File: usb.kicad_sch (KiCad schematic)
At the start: 11 parts, among them J3 CX90B1-24P, U3 CY7C65215-32LTXI, U8 TPD4E004DRYR

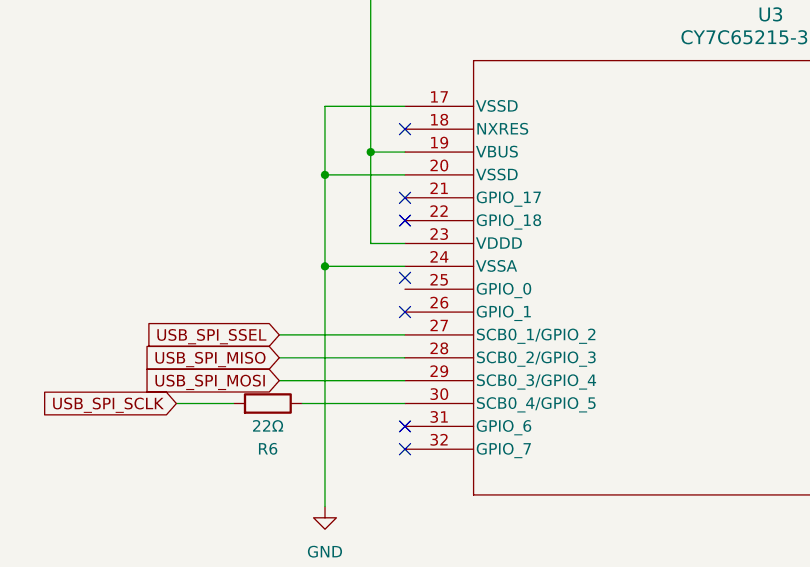
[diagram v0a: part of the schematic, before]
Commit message: Clean up schematics
Signed-off-by: Corey Minyard <corey@minyard.net>
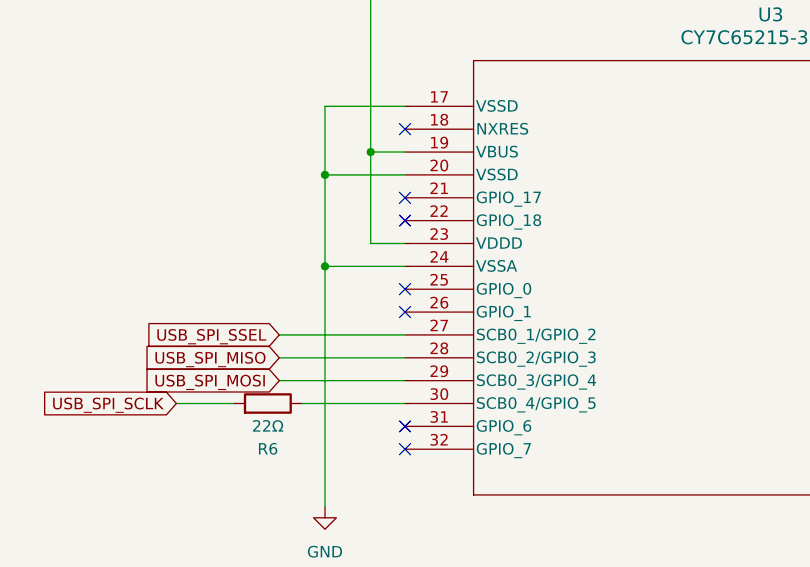
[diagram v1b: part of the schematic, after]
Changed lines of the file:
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@@
 	)
 	(no_connect
-		(at 55.88 116.84)
+		(at 55.88 118.11)
 	)
 	(no_connect
@@
 		(pin "11"
 		)
-	)
+		(instances
+			(project ""
+				(path "/23e49ab9-97e0-460a-806c-ff6f37958474/a401ed87-a6b2-451c-b983-d48d83161fe4"
+					(reference "U3")
+					(unit 1)
+				)
+			)
+		)
+	)

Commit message: Start on PCB
Clean up a lot of issues.

Signed-off-by: Corey Minyard <corey@minyard.net>
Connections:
- net GND: now also U3.33 (GND/PAD)
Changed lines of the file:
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@@
+	)
+	(junction
+		(at 46.99 97.79)
+		(diameter 0)
+		(color 0 0 0 0)
 	)
 	(junction
@@
 		(pts
 			(xy 137.16 107.95) (xy 151.13 107.95)
+		)
+		(stroke
+			(width 0)
+			(type default)
+		)
+	)
+	(wire
+		(pts
+			(xy 55.88 95.25) (xy 46.99 95.25)
+		)
+		(stroke
+			(width 0)
+			(type default)
+		)
+	)
+	(wire
+		(pts
+			(xy 46.99 95.25) (xy 46.99 97.79)
 		)
 		(stroke
@@
 		(pin "11"
 		)
+		(pin "33"
+		)
 		(instances

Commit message: Finish layout
Signed-off-by: Corey Minyard <corey@minyard.net>
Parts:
- added C82, C83, C84: 100nF, Capacitor_SMD:C_0402_1005Metric, symbol Device:C
- added R21, R22: 0Ω, Resistor_SMD:R_0402_1005Metric, symbol Device:R
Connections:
- net +3.3V: now also C82.2, C83.2, C84.2
- net GND: now also C82.1, C83.1, C84.1
- net USB_RX: now also R22.2; no longer U3.5 (SCB1_0/GPIO_10)
- net USB_TX: now also R21.2; no longer U3.6 (SCB1_1/GPIO_11)
- new net: R22.1, U3.5 (SCB1_0/GPIO_10)
- new net: R21.1, U3.6 (SCB1_1/GPIO_11)

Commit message: Add pull up on the PA enables
So they are off by default.

Signed-off-by: Corey Minyard <corey@minyard.net>
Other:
- note added: "Main USB connector. If the connection is capable of supplying 3A at 5V, you can use this for power by installing J9."
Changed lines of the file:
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@@
+		)
+	)
+	(text "Main USB connector.  If the\nconnection is capable of\nsupplying 3A at 5V, you can\nuse this for power by installing\nJ9."
+		(exclude_from_sim no)
+		(at 213.614 33.528 0)
+		(effects
+			(font
+				(size 1.27 1.27)
+			)
 		)
 	)

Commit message: Make a bunch of GPIOs more easily available
Put them on DNP zero-ohm resistors.

Signed-off-by: Corey Minyard <corey@minyard.net>
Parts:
- added R41, R42: 0Ω, Resistor_SMD:R_0402_1005Metric, symbol Device:R
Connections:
- net at U3.25 (GPIO_0): now also R41.1
- net at U3.26 (GPIO_1): now also R42.1
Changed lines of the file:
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@@
 	)
 	(no_connect
-		(at 55.88 120.65)
-	)
-	(no_connect
 		(at 194.31 62.23)
 	)
@@
 	)
 	(no_connect
+		(at 35.56 118.11)
+	)
+	(no_connect
 		(at 137.16 115.57)
 	)
@@
 	)
 	(no_connect
-		(at 55.88 118.11)
+		(at 35.56 120.65)
 	)
 	(no_connect
@@
 	(wire
 		(pts
+			(xy 43.18 120.65) (xy 55.88 120.65)
+		)
+		(stroke
+			(width 0)
+			(type default)
+		)
+	)
+	(wire
+		(pts
 			(xy 46.99 115.57) (xy 55.88 115.57)
 		)
@@
 	(wire
 		(pts
+			(xy 43.18 118.11) (xy 55.88 118.11)
+		)
+		(stroke
+			(width 0)
+			(type default)
+		)
+	)
+	(wire
+		(pts
 			(xy 148.59 88.9) (xy 148.59 91.44)
 		)
@@
 	)
 	(symbol
+		(lib_id "Device:R")
+		(at 39.37 118.11 270)
+		(unit 1)
+		(exclude_from_sim no)
+		(in_bom no)
+		(on_board yes)
+		(dnp yes)
+		(property "Reference" "R41"
+			(at 34.544 116.586 90)
+			(effects
+				(font
+					(size 1.27 1.27)
+				)
+			)
+		)
+		(property "Value" "0Ω"
+			(at 43.688 116.586 90)
+			(effects
+				(font
+					(size 1.27 1.27)
+				)
+			)
+		)
+		(property "Footprint" "Resistor_SMD:R_0402_1005Metric"
+			(at 39.37 116.332 90)
+			(effects
+				(font
+					(size 1.27 1.27)
+				)
+				(hide yes)
+			)
+		)
+		(property "Datasheet" "~"
+			(at 39.37 118.11 0)
+			(effects
+				(font
+					(size 1.27 1.27)
+				)
+				(hide yes)
+			)
+		)
+		(property "Description" "Resistor"
+			(at 39.37 118.11 0)
+			(effects
+				(font
+					(size 1.27 1.27)
+				)
+				(hide yes)
+			)
+		)
+		(pin "2"
+		)
+		(pin "1"
+		)
+		(instances
+			(project "FSKGroundStation"
+				(path "/23e49ab9-97e0-460a-806c-ff6f37958474/a401ed87-a6b2-451c-b983-d48d83161fe4"
+					(reference "R41")
+					(unit 1)
+				)
+			)
+		)
+	)
+	(symbol
 		(lib_id "power:GND")
 		(at 177.8 83.82 0)
@@
 					(unit 1)
 				)
+			)
+		)
+	)
+	(symbol
+		(lib_id "Device:R")
+		(at 39.37 120.65 270)
+		(unit 1)
+		(exclude_from_sim no)
+		(in_bom no)
+		(on_board yes)
+		(dnp yes)
+		(property "Reference" "R42"
+			(at 34.544 119.126 90)
+			(effects
+				(font
+					(size 1.27 1.27)
+				)
+			)
+		)
+		(property "Value" "0Ω"
+			(at 43.688 119.126 90)
+			(effects
+				(font
+					(size 1.27 1.27)
+				)
+			)
+		)
+		(property "Footprint" "Resistor_SMD:R_0402_1005Metric"
+			(at 39.37 118.872 90)
+			(effects
+				(font
+					(size 1.27 1.27)
+				)
+				(hide yes)
+			)
+		)
+		(property "Datasheet" "~"
+			(at 39.37 120.65 0)
+			(effects
+				(font
+					(size 1.27 1.27)
+				)
+				(hide yes)
+			)
+		)
+		(property "Description" "Resistor"
+			(at 39.37 120.65 0)
+			(effects
+				(font
+					(size 1.27 1.27)
+				)
+				(hide yes)
+			)
+		)
+		(pin "2"
+		)
+		(pin "1"
+		)
+		(instances
+			(project "FSKGroundStation"
+				(path "/23e49ab9-97e0-460a-806c-ff6f37958474/a401ed87-a6b2-451c-b983-d48d83161fe4"
+					(reference "R42")
+					(unit 1)
+				)

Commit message: Finish initial layet
Signed-off-by: Corey Minyard <corey@minyard.net>
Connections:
- net USB_SPI_DATA_READY: no longer names the net of U3.2 (SCB0_0/GPIO_8)
- no-connect marks 23 -> 24
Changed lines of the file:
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@@
+	)
+	(no_connect
+		(at 137.16 133.35)
 	)
 	(no_connect
@@
 		(pts
 			(xy 246.38 44.45) (xy 217.17 44.45)
-		)
-		(stroke
-			(width 0)
-			(type default)
-		)
-	)
-	(wire
-		(pts
-			(xy 137.16 133.35) (xy 151.13 133.35)
 		)
 		(stroke
@@
 				(hide yes)
 			)
-		)
-	)
-	(global_label "USB_SPI_DATA_READY"
-		(shape input)
-		(at 151.13 133.35 0)
-		(fields_autoplaced yes)
-		(effects
-			(font
-				(size 1.27 1.27)
-			)
-			(justify left)
-		)
-		(property "Intersheetrefs" "${INTERSHEET_REFS}"
-			(at 174.1933 133.35 0)
-			(effects
-				(font
-					(size 1.27 1.27)
-				)
-				(justify left)
-				(hide yes)
-			)

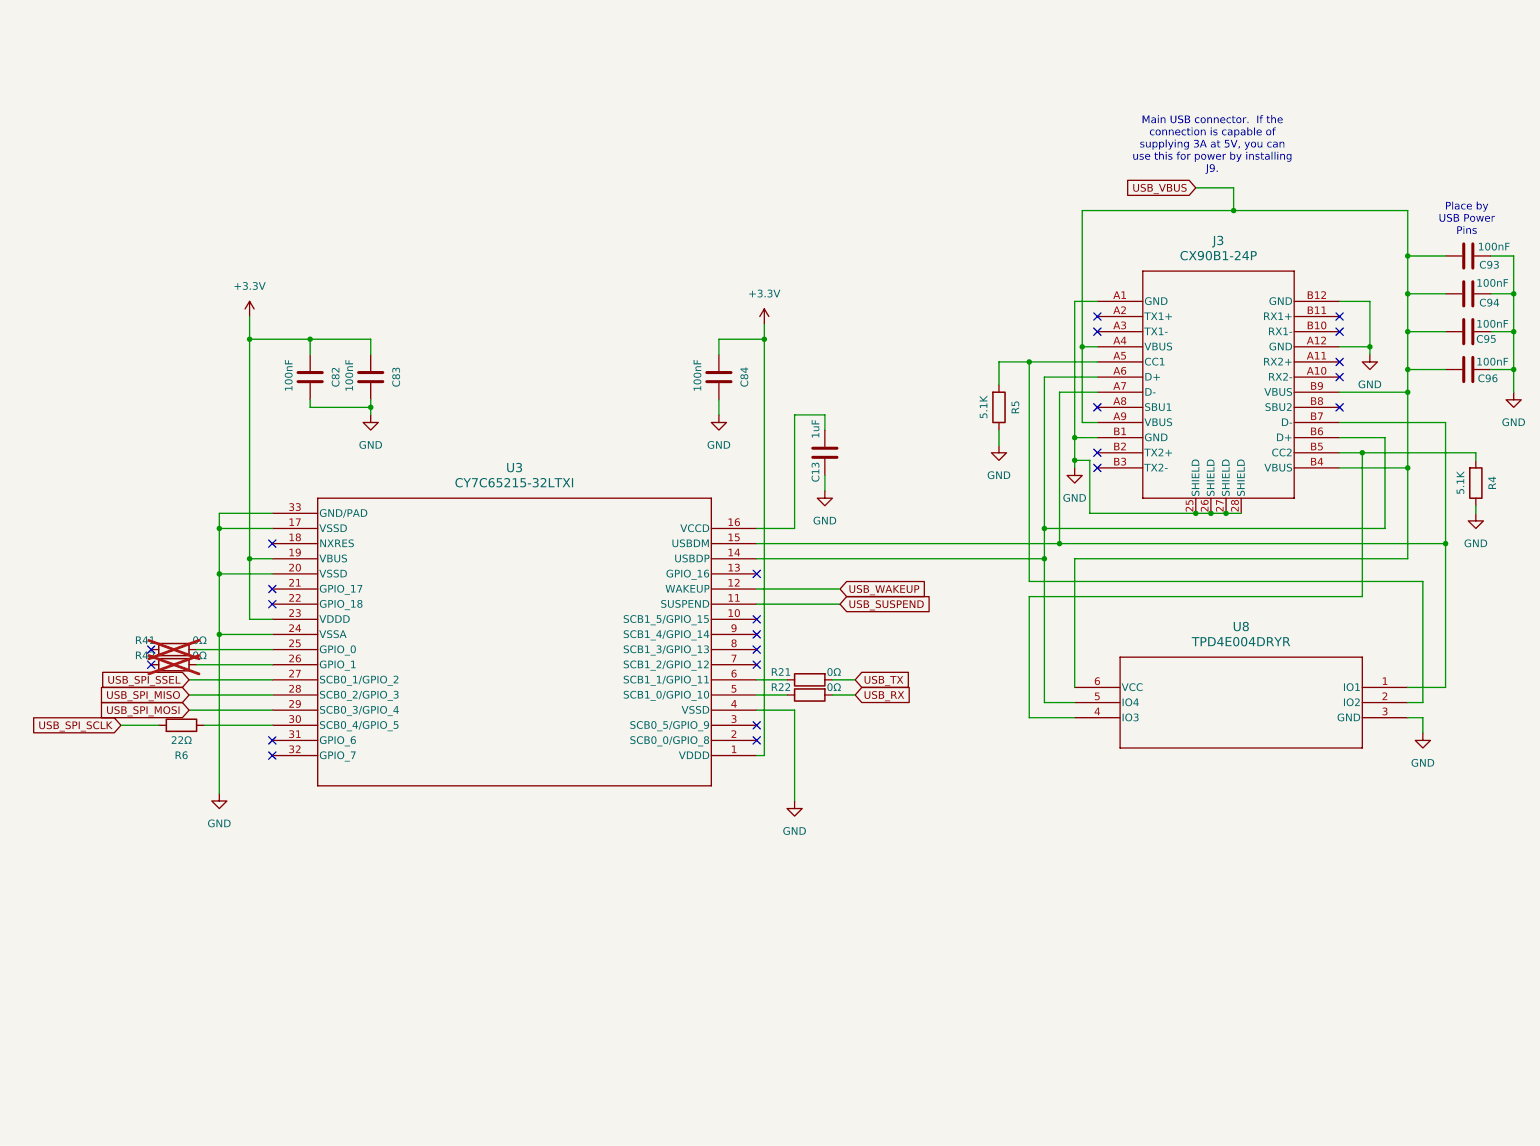
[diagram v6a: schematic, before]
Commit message: Switch to a CPU with a USB interface for the USB connection
The part that was picked had proprietary tools and configuration and it
didn't support interrupts.  The CPU is cheaper and more capable.

Signed-off-by: Corey Minyard <corey@minyard.net>
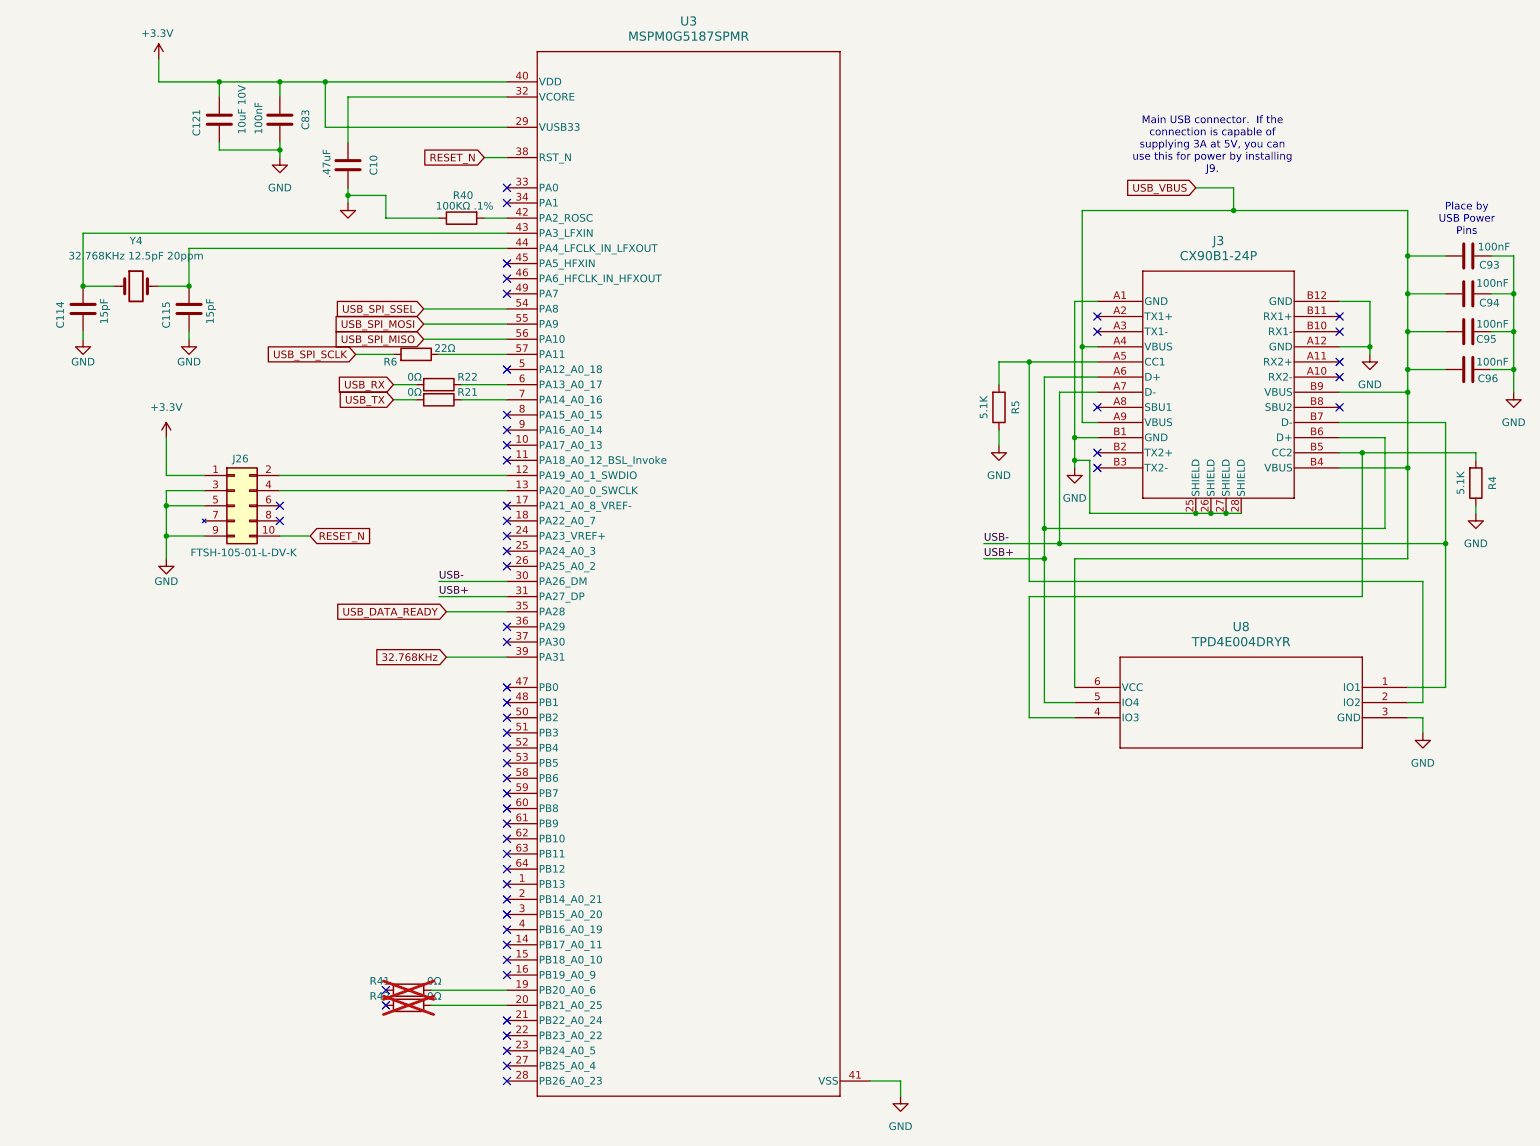
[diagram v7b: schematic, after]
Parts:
- removed C13: 1uF, Capacitor_SMD:C_0603_1608Metric_Pad1.08x0.95mm_HandSolder, symbol Device:C
- removed C82, C84: 100nF, Capacitor_SMD:C_0402_1005Metric, symbol Device:C
- removed U3: CY7C65215-32LTXI, footprints:PG-VQFN-32-803, symbol Local ICs:CY7C65215-32LTXI
- added C10: .47uF, Capacitor_SMD:C_0603_1608Metric_Pad1.08x0.95mm_HandSolder, symbol Device:C
- added C114, C115: 15pF, Capacitor_SMD:C_0402_1005Metric_Pad0.74x0.62mm_HandSolder, symbol Device:C
- added C121: 10uF 10V, Capacitor_SMD:C_1206_3216Metric_Pad1.33x1.80mm_HandSolder, symbol Device:C
- added J26: FTSH-105-01-L-DV-K, footprints:FTSH-105-01-L-DV-K, symbol Local Connectors:ARM CM10 JTAG
- added R40: 100KΩ .1%, Resistor_SMD:R_0402_1005Metric, symbol Device:R
- added U3: MSPM0G5187SPMR, footprints:PM0064A-IPC_A, symbol Local ICs:MSPM0G5187SPMR
- added Y4: 32.768KHz 12.5pF 20ppm, Crystal:Crystal_SMD_2012-2Pin_2.0x1.2mm, symbol Device:Crystal
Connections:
- net +3.3V: now also C121.2, J26.1 (VTREF), U3.29 (VUSB33), U3.40 (VDD)
- net GND: now also C10.1, C114.1, C115.1, C121.1, J26.3 (GND), J26.5 (GND), J26.9 (GND), R40.1, U3.41 (VSS)
- net USB_SPI_MISO: now also U3.56 (PA10)
- net USB_SPI_MOSI: now also U3.55 (PA9)
- net USB_SPI_SSEL: now also U3.54 (PA8)
- net USB+: now reaches J3.A6 (D+), J3.B6 (D+), U8.5 (IO4)
- net USB+: now also U3.31 (PA27_DP)
- net USB-: now reaches J3.A7 (D-), J3.B7 (D-), U8.1 (IO1)
- net USB-: now also U3.30 (PA26_DM)
- net at R41.1: now also U3.19 (PB20_A0_6)
- net at R42.1: now also U3.20 (PB21_A0_25)
- net at R6.1: now also U3.57 (PA11)
- net at R22.1: now also U3.6 (PA13_A0_17)
- net at R21.1: now also U3.7 (PA14_A0_16)
- new net: J26.2 (TMS), U3.12 (PA19_A0_1_SWDIO)
- new net: J26.4 (TCK), U3.13 (PA20_A0_0_SWCLK)
- new net: C115.2, U3.44 (PA4_LFCLK_IN_LFXOUT), Y4.2
- new net: C10.2, U3.32 (VCORE)
- new net: C114.2, U3.43 (PA3_LFXIN), Y4.1
- new net: R40.2, U3.42 (PA2_ROSC)
- new net 32.768KHz: U3.39 (PA31)
- new net RESET_N: J26.10 (NRST), U3.38 (RST_N)
- new net USB_DATA_READY: U3.35 (PA28)
- no-connect marks 24 -> 56
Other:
- moved on the sheet: C83, R21, R22, R41, R42, R6

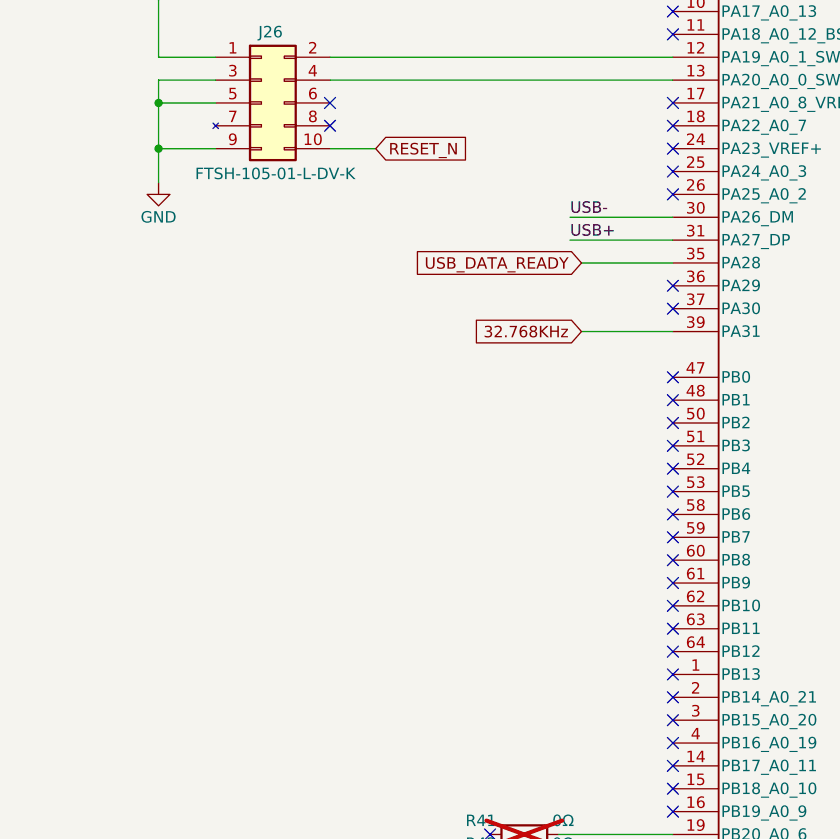
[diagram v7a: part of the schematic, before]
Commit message: Add a clock from the USB chip to the FPGA
The FPGA might need a clock for certain things, so provide it.

Signed-off-by: Corey Minyard <corey@minyard.net>
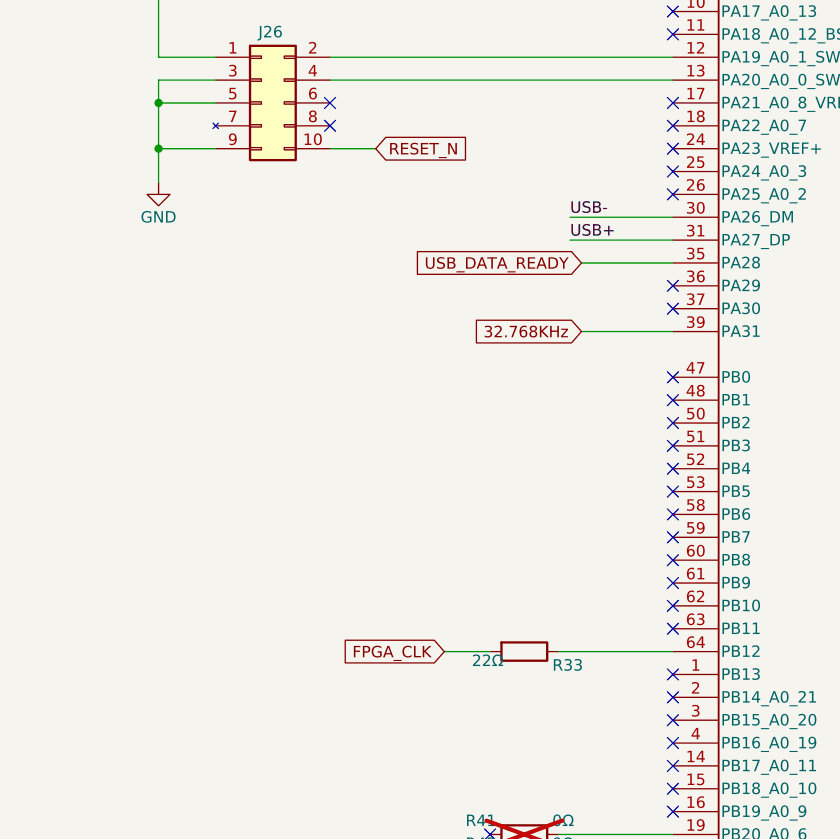
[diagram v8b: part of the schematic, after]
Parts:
- added R33: 22Ω, Resistor_SMD:R_0402_1005Metric_Pad0.72x0.64mm_HandSolder, symbol Device:R
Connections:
- net at U3.64 (PB12): now also R33.1
- new net FPGA_CLK: R33.2
- no-connect marks 56 -> 55
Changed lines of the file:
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@@
-	)
-	(no_connect
-		(at 95.25 154.94)
 	)
 	(no_connect
@@
 	(wire
 		(pts
+			(xy 69.85 154.94) (xy 74.93 154.94)
+		)
+		(stroke
+			(width 0)
+			(type default)
+		)
+	)
+	(wire
+		(pts
 			(xy 238.76 85.09) (xy 257.81 85.09)
 		)
@@
 		(pts
 			(xy 95.25 50.8) (xy 41.91 50.8)
+		)
+		(stroke
+			(width 0)
+			(type default)
+		)
+	)
+	(wire
+		(pts
+			(xy 82.55 154.94) (xy 95.25 154.94)
 		)
 		(stroke
@@
 		(property "Intersheetrefs" "${INTERSHEET_REFS}"
 			(at 66.2601 76.2 0)
+			(effects
+				(font
+					(size 1.27 1.27)
+				)
+				(justify right)
+				(hide yes)
+			)
+		)
+	)
+	(global_label "FPGA_CLK"
+		(shape input)
+		(at 69.85 154.94 180)
+		(fields_autoplaced yes)
+		(effects
+			(font
+				(size 1.27 1.27)
+			)
+			(justify right)
+		)
+		(property "Intersheetrefs" "${INTERSHEET_REFS}"
+			(at 57.6119 154.94 0)
 			(effects
 				(font
@@
 					(size 1.27 1.27)
 				)
+				(hide yes)
 			)
 		)
@@
 					(unit 1)
 				)
+			)
+		)
+	)
+	(symbol
+		(lib_id "Device:R")
+		(at 78.74 154.94 270)
+		(unit 1)
+		(exclude_from_sim no)
+		(in_bom yes)
+		(on_board yes)
+		(dnp no)
+		(property "Reference" "R33"
+			(at 83.566 156.464 90)
+			(effects
+				(font
+					(size 1.27 1.27)
+				)
+			)
+		)
+		(property "Value" "22Ω"
+			(at 74.676 155.956 90)
+			(effects
+				(font
+					(size 1.27 1.27)
+				)
+			)
+		)
+		(property "Footprint" "Resistor_SMD:R_0402_1005Metric_Pad0.72x0.64mm_HandSolder"
+			(at 78.74 153.162 90)
+			(effects
+				(font
+					(size 1.27 1.27)
+				)
+				(hide yes)
+			)
+		)
+		(property "Datasheet" "~"
+			(at 78.74 154.94 0)
+			(effects
+				(font
+					(size 1.27 1.27)
+				)
+				(hide yes)
+			)
+		)
+		(property "Description" "Resistor"
+			(at 78.74 154.94 0)
+			(effects
+				(font
+					(size 1.27 1.27)
+				)
+				(hide yes)
+			)
+		)
+		(pin "2"
+		)
+		(pin "1"
+		)
+		(instances
+			(project "FSKGroundStation"
+				(path "/23e49ab9-97e0-460a-806c-ff6f37958474/a401ed87-a6b2-451c-b983-d48d83161fe4"
+					(reference "R33")
+					(unit 1)
+				)
